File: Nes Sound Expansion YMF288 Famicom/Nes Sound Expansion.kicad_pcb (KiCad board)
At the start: 2 copper layers, 66 x 86.4 mm, 31 parts, among them J1 OUT, J2 EXP 1-30, J3 EXP 1-30, J4 31-60, J8 EXP 25-48, J9 EXP 1-24, U1 74LS139, U10 74LS257, U2 74LS132, U6 74LS174, U7 74LS174, U8 74LS257, U9 74LS257, X1 CXO_DIP8

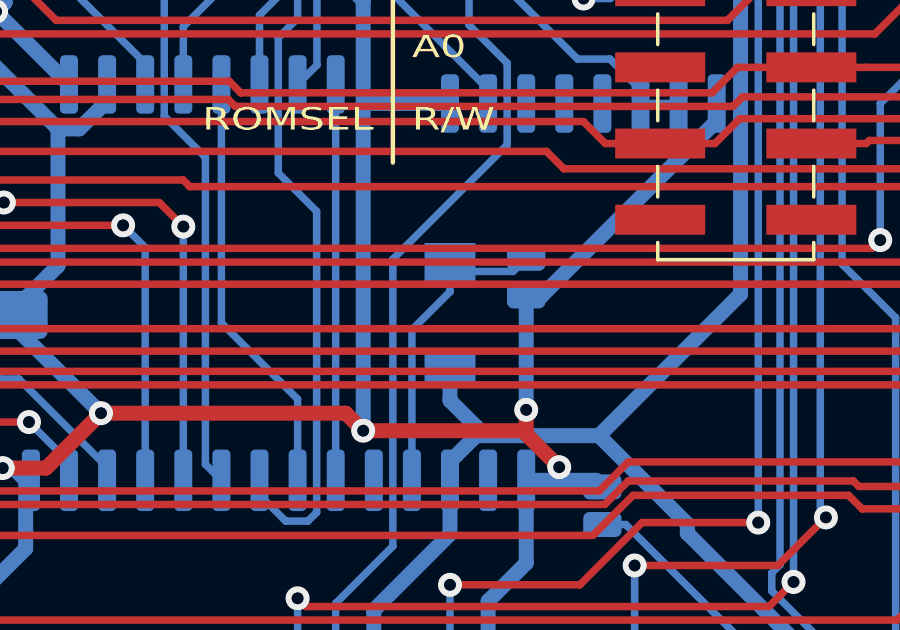
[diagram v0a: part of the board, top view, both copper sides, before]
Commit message: changed reset circuit
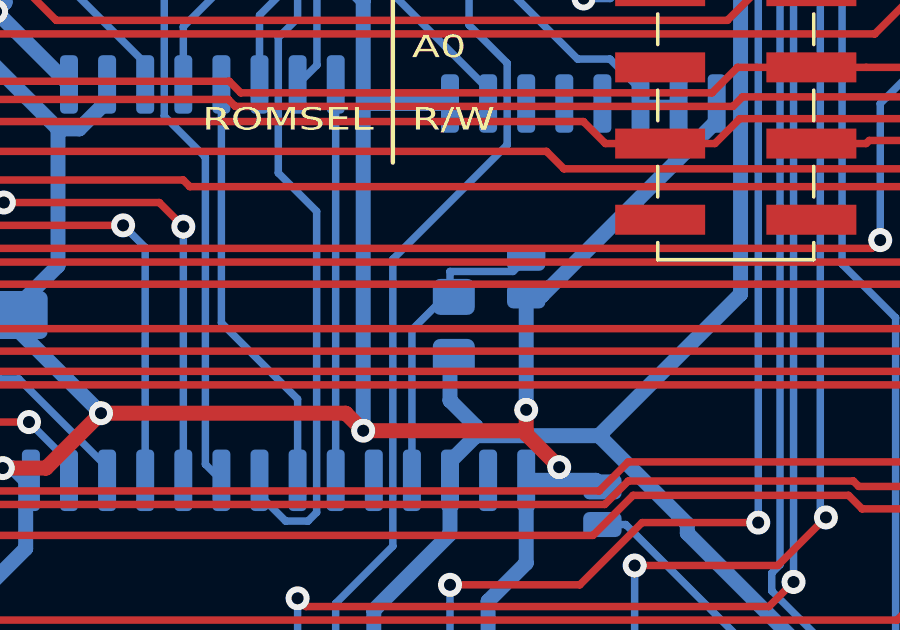
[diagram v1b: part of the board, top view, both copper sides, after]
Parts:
- removed D1: 1N4148, Diode_SMD:D_MiniMELF
- added R4: 1k, Resistor_SMD:R_0805_2012Metric_Pad1.20x1.40mm_HandSolder, B.Cu at (106.2, 86.1)
- C1: value 68pF -> 10uF

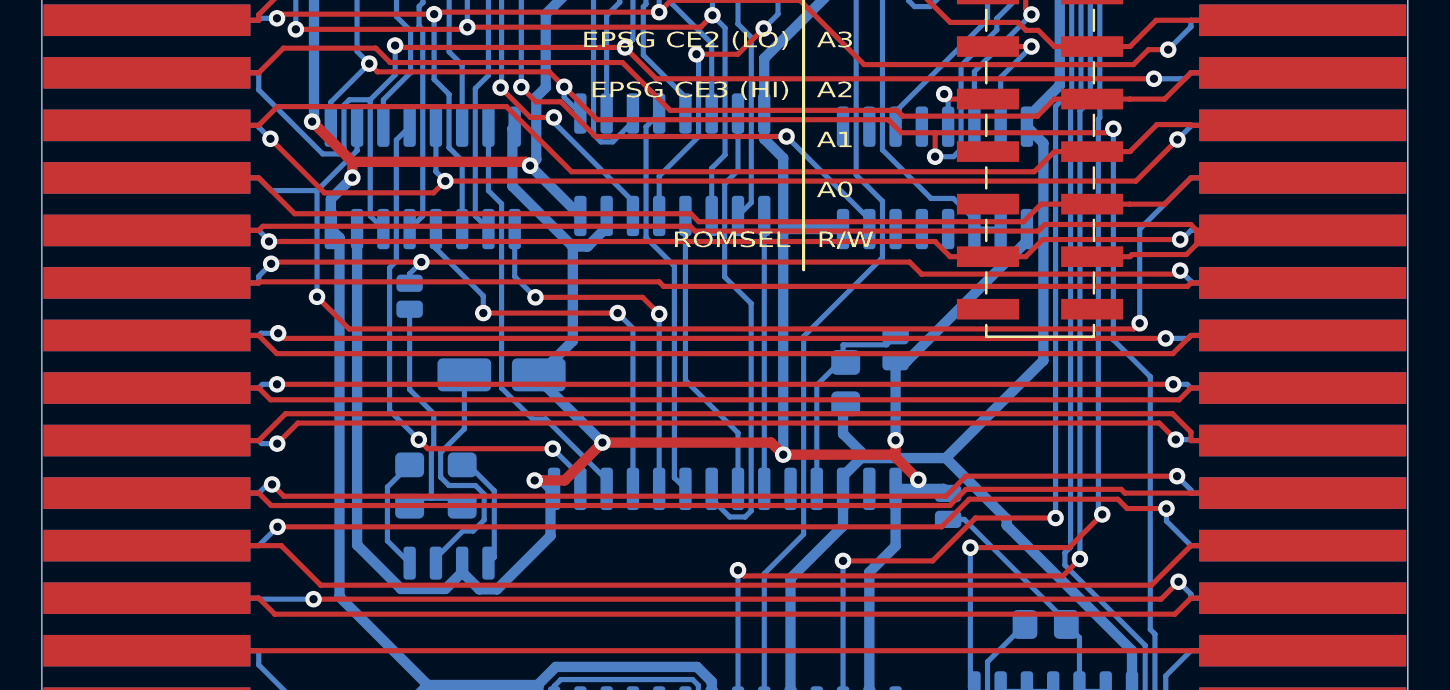
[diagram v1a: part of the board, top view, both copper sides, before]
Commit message: Updated mixing on the Famicom version
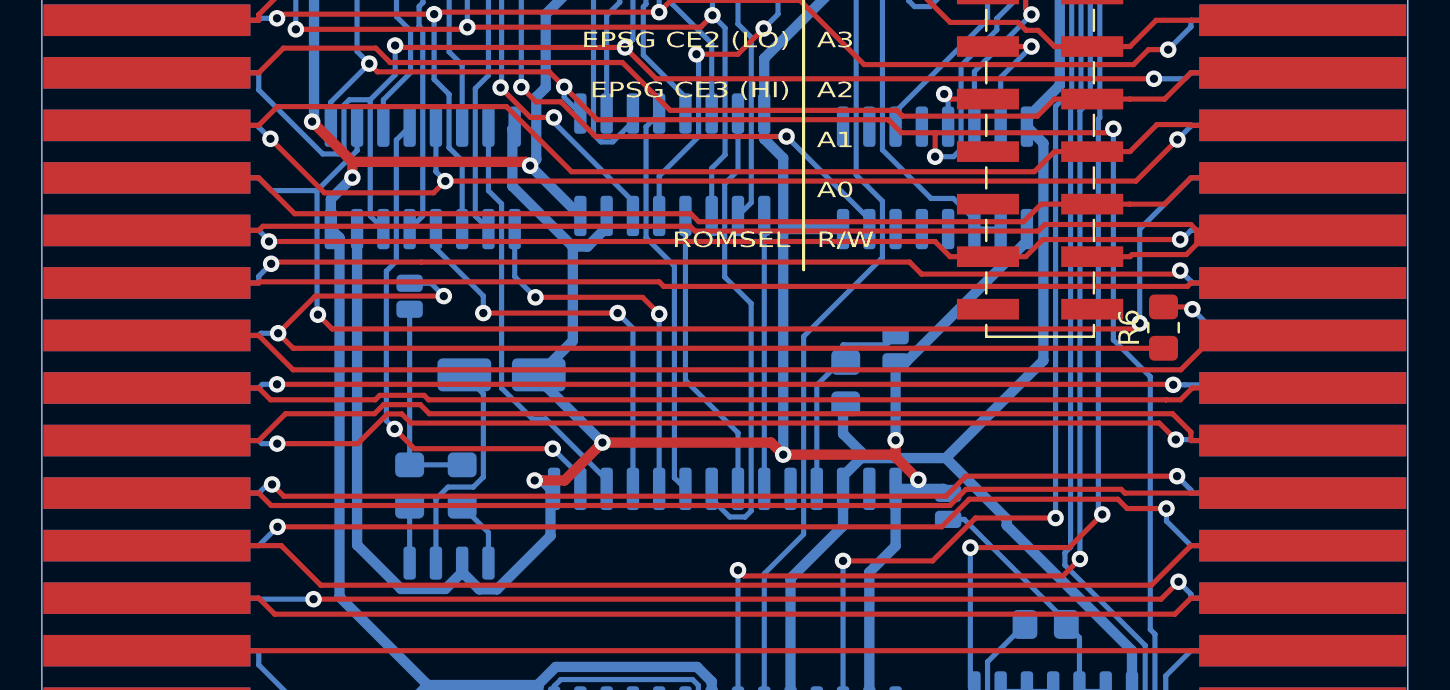
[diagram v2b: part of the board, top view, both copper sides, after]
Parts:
- added R6: 3k, Resistor_SMD:R_0805_2012Metric_Pad1.20x1.40mm_HandSolder, F.Cu at (121.5, 83.4)
- turned R5 to 90 degrees
- turned R8 to 270 degrees
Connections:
- C6 pad 2: Aud -> AudIn
- J4 pad 16: AudIn -> Net-(J4-Pad16)
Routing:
- net Net-(J4-Pad16): track 0.00 -> 7.30 mm, vias 0 -> 1
- net Net-(BU9480F1-Pad1): track 5.64 -> 2.75 mm
- net Net-(C6-Pad1): track 12.5 -> 10.1 mm
- net GND1: track 61.7 -> 59.8 mm
- net AudIn: track 61.2 -> 63.0 mm
- net Net-(BU9480F1-Pad4): track 5.68 -> 3.82 mm
- net Net-(BU9480F1-Pad2): track 12.5 -> 11.2 mm
- net Aud: track 63.4 -> 62.2 mm, vias 3 -> 2
- net D0_Chip: track 25.3 -> 25.8 mm

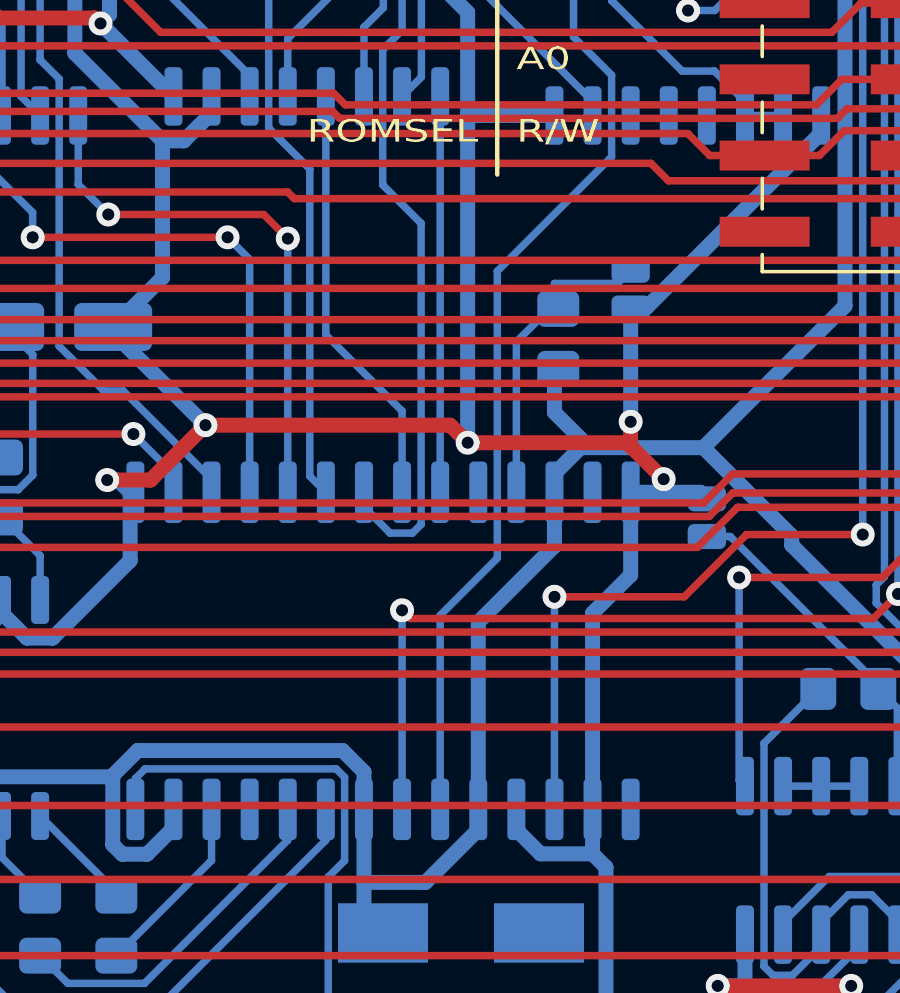
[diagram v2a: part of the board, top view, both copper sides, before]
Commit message: Added IRQ from the YMF288
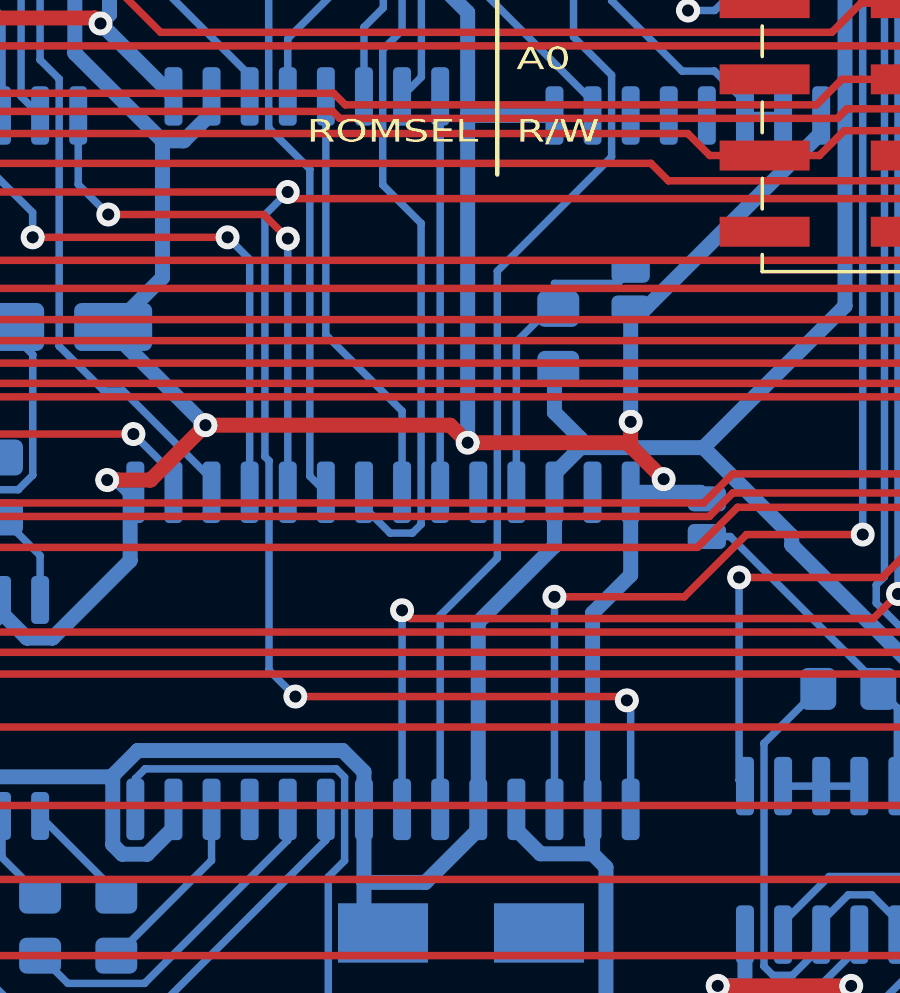
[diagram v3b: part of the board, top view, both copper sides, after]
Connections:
- YMF288 pad 15: Net-(YMF288-Pad15) -> IRQ
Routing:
- net IRQ: track 61.1 -> 93.5 mm, vias 0 -> 3

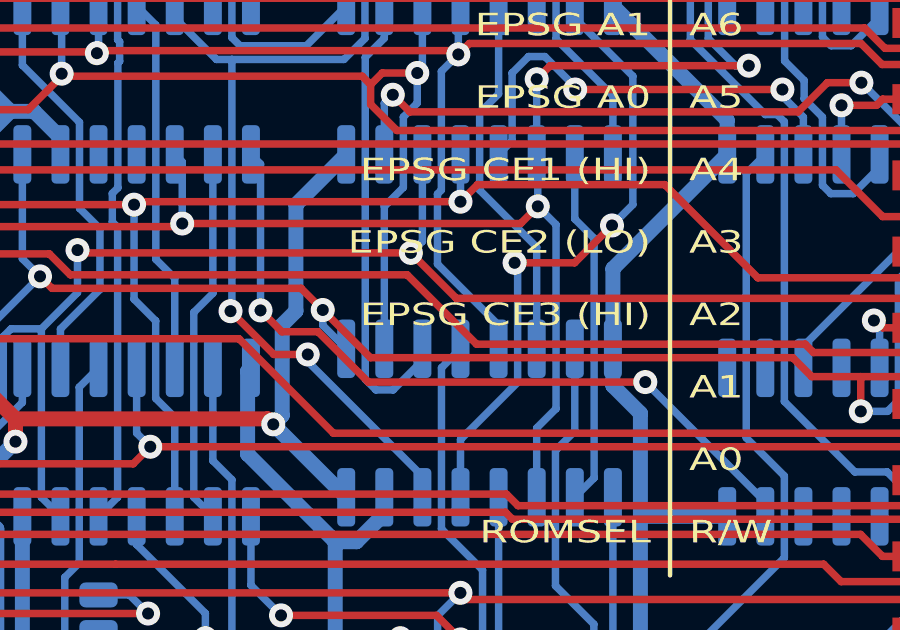
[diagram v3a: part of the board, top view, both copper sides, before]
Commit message: Added logo, 3.5mm 3d module, removed unused stuff
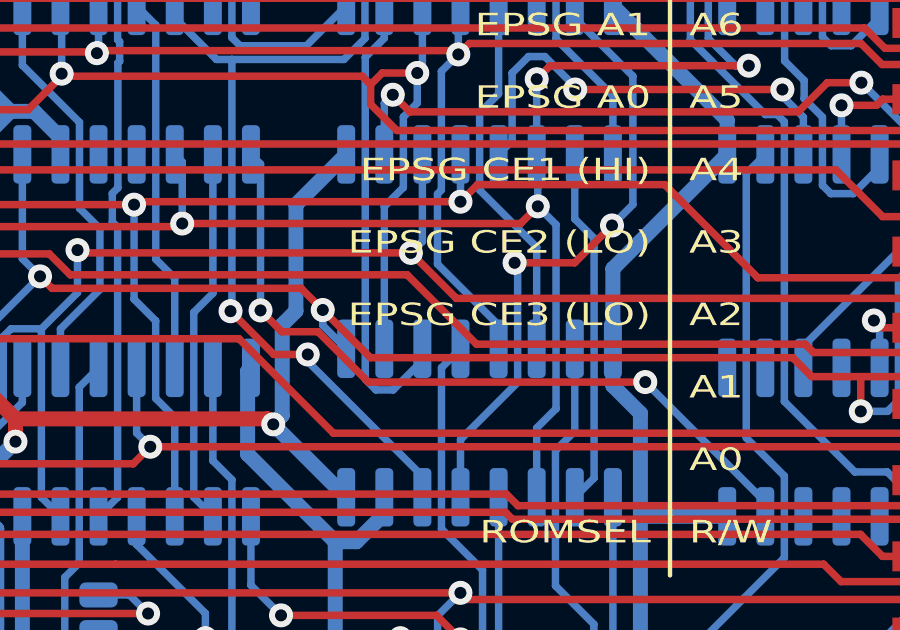
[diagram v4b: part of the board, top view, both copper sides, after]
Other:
- board text added: "5V A12 A13 A14 EPSG A1 EPSG A0 EPSG CE1 (HI) EPSG CE2 (LO) EPSG CE3 (LO) ROMSEL"
- board text removed: "5V A12 A13 A14 EPSG A1 EPSG A0 EPSG CE1 (HI) EPSG CE2 (LO) EPSG CE3 (HI) ROMSEL"

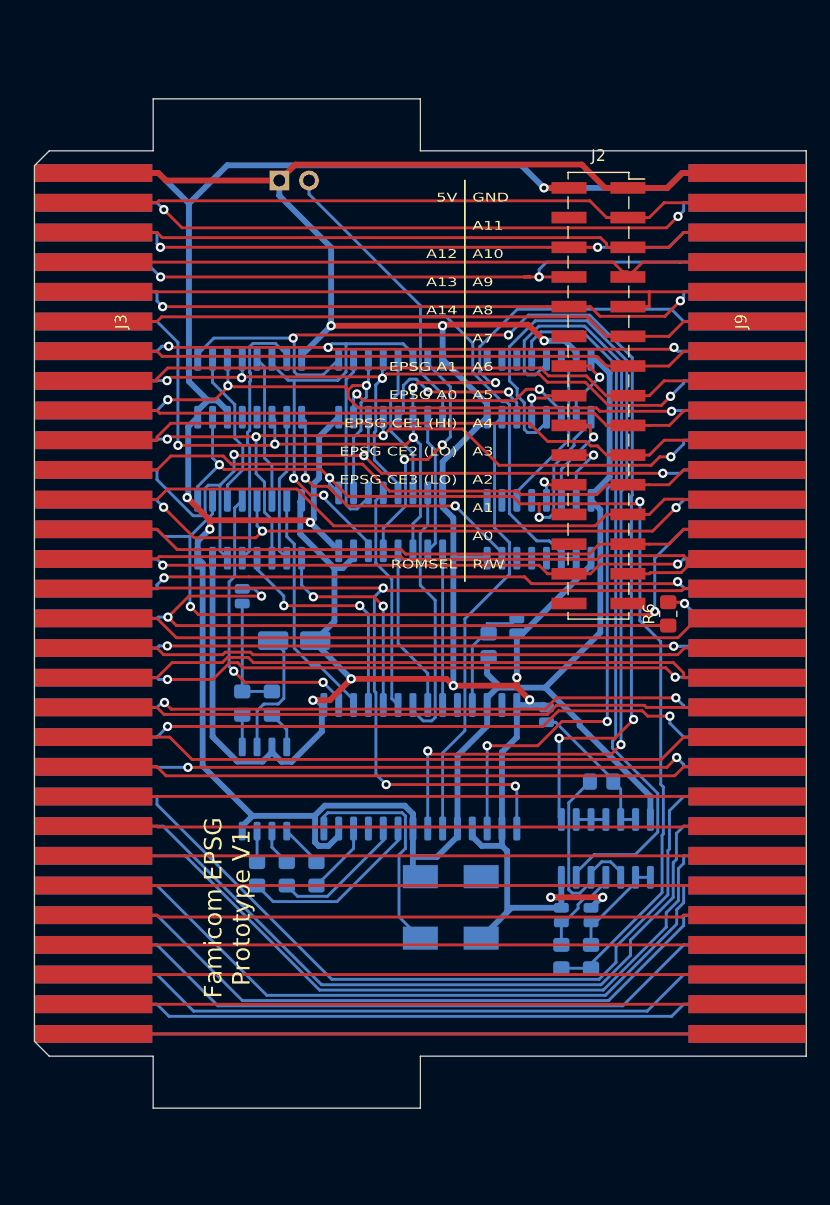
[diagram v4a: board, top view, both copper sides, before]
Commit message: Redesigned to fit a Famicom MMC cart and updated readme
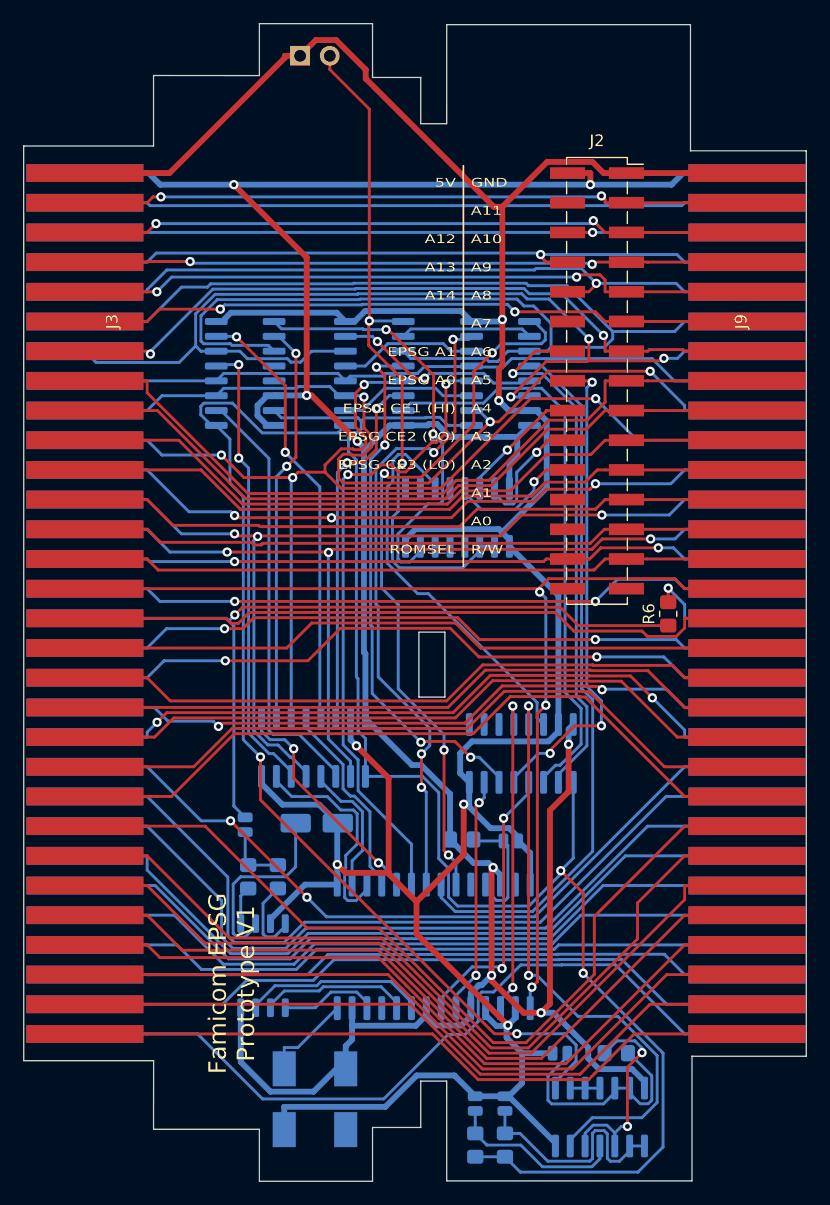
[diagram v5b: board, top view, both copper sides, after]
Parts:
- removed R1, R2, R3: 1k, Resistor_SMD:R_0805_2012Metric_Pad1.20x1.40mm_HandSolder
- moved U10 31.3 mm to (109.0, 95.4)
- moved C5 29.0 mm to (112.3, 121.0), turned to 0 degrees
- moved R14 23.3 mm to (117.1, 121.0)
- moved U2 23.0 mm to (115.7, 126.5)
- moved X1 20.1 mm to (91.3, 125.0), turned to 180 degrees
- moved C6 19.6 mm to (85.3, 101.5)
- moved U9 19.5 mm to (91.2, 94.9), turned to 90 degrees
- moved C1 18.4 mm to (108.1, 102.9), turned to 180 degrees
- moved R12 17.7 mm to (105.0, 128.9)
- moved R13 17.7 mm to (107.6, 128.9)
- moved C3 17.7 mm to (105.0, 125.3)
- moved C4 17.7 mm to (107.6, 125.3)
- moved R4 16.8 mm to (103.9, 102.7), turned to 0 degrees
- moved U8 15.8 mm to (107.2, 62.9), turned to 0 degrees
- moved C2 15.7 mm to (91.5, 101.3)
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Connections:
- J2 pad 12: Net-(J2-Pad12) -> (no net)
- J2 pad 24: Net-(J2-Pad24) -> (no net)
- J2 pad 26: Net-(J2-Pad26) -> (no net)
- J2 pad 29: Net-(J2-Pad29) -> (no net)
- J2 pad 30: Net-(J2-Pad30) -> (no net)
- J2 pad 4: Net-(J2-Pad4) -> (no net)
- U1 pad 10: Net-(U1-Pad10) -> (no net)
- U1 pad 12: Net-(U1-Pad12) -> (no net)
- U1 pad 4: Net-(U1-Pad4) -> (no net)
- U1 pad 5: Net-(U1-Pad5) -> (no net)
- U1 pad 6: Net-(U1-Pad6) -> (no net)
- U1 pad 9: Net-(U1-Pad9) -> (no net)
- U10 pad 10: Net-(U10-Pad10) -> (no net)
- U10 pad 11: Net-(U10-Pad11) -> (no net)
- U10 pad 9: Net-(U10-Pad9) -> (no net)
- U7 pad 12: Net-(U7-Pad12) -> (no net)
- U7 pad 13: Net-(U7-Pad13) -> (no net)
- X1 pad 1: Net-(X1-Pad1) -> (no net)
- YMF288 pad 10: Net-(YMF288-Pad10) -> (no net)
- YMF288 pad 13: Net-(YMF288-Pad13) -> (no net)
- YMF288 pad 23: Net-(R3-Pad2) -> Net-(BU9480F1-Pad7)
- YMF288 pad 24: Net-(R2-Pad2) -> Net-(BU9480F1-Pad6)
- YMF288 pad 25: Net-(YMF288-Pad25) -> (no net)
- YMF288 pad 26: Net-(R1-Pad2) -> Net-(BU9480F1-Pad5)
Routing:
- net A1_Chip: track 79.5 -> 24.1 mm
- net D7_Chip: track 13.2 -> 61.7 mm, vias 0 -> 4
- net D6_Chip: track 14.2 -> 61.1 mm
- net Addr_A1: track 7.37 -> 45.5 mm
- net Addr_A13: track 4.92 -> 42.1 mm, vias 1 -> 3
- net D4_Chip: track 19.2 -> 54.7 mm, vias 0 -> 2
- net D5_Chip: track 22.9 -> 55.9 mm, vias 0 -> 4
- net CS_Chip: track 59.3 -> 27.9 mm
- net A0_buf: track 15.1 -> 45.4 mm, vias 2 -> 4
- net A1_buf: track 21.5 -> 49.3 mm, vias 2 -> 0
- net D7: track 94.9 -> 122.0 mm, vias 5 -> 0
- net D1_buf: track 12.6 -> 39.3 mm, vias 0 -> 2
- net 4016_EN: track 105.1 -> 129.6 mm, vias 4 -> 2
- net D0_buf: track 13.7 -> 37.1 mm
- net GND: track 269.6 -> 291.9 mm, vias 10 -> 6
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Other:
- board size 66 x 86.4 mm -> 67 x 99 mm

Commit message: minor updates
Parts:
- moved J1 8.35 mm to (96.0, 41.5), turned to 180 degrees
- moved R6 3.60 mm to (118.0, 84.1), turned to 0 degrees
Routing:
- net OUT1: track 59.1 -> 49.3 mm
- net GND: track 291.9 -> 286.3 mm
- net AudIn: track 68.5 -> 63.8 mm
- net +5V: track 249.7 -> 246.9 mm
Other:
- outline, holes or cut-outs redrawn
- net class Power: trace_width 0.5 -> 0.8
- board text added: "1 2 3 4 5 6 7 8 9 10 11 12 13 14 15 16 17 18 19 20 21 22 23 24 25 26 27 28 29 30"
- board text added: "31 32 33 34 35 36 37 38 39 40 41 42 43 44 45 46 47 48 49 50 51 52 53 54 55 56 57 58 59 60"
- board text added: "Famicom EPSM REV.A"
- board text removed: "Famicom EPSG Prototype V1"
